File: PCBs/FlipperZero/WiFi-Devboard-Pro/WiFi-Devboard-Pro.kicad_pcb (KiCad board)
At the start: 2 copper layers, 78.5 x 20.1 mm, 46 parts, among them IC1 ESP32-WROOM-32E-N4, IC2 DMP1045U-7, IC3 AZ1117H-3.3TRE1, IC4 DMP1045U-7, IC5 DMP1045U-7, J1 3220-10-0300-00, J2 X6511WVS-08H-C60D48R2, J3 DZ254S-11-10-48, J4 Conn_01x11, J5 Conn_01x11, J6 503398-1892, U1 MMDT2907A-7-F, U2 MMDT2907A-7-F, U3 MMDT2907A-7-F

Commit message: started review
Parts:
- moved R6 1.29 mm to (150.1, 104.9), turned to 180 degrees
- moved C7 0.95 mm to (116.5, 92.3)
- moved R3 0.89 mm to (119.9, 91.9)
- moved C9 0.15 mm to (134.4, 99.5)
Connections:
- J4 pad 1: +3V3 -> GND
- J4 pad 2: GND -> +3V3
- J5 pad 1: GPIO25 -> GND
- J5 pad 10: GND -> RX
- J5 pad 11: +5V -> TX
- J5 pad 2: GPIO26 -> +5V
- J5 pad 3: GPIO27 -> GPIO25
- J5 pad 4: GPIO32 -> GPIO26
- J5 pad 5: GPIO33 -> GPIO27
- J5 pad 6: GPIO34 -> GPIO32
- J5 pad 7: GPIO35 -> GPIO33
- J5 pad 8: RX -> GPIO34
- J5 pad 9: TX -> GPIO35
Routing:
- net +5V: track 65.4 -> 33.9 mm, vias 2 -> 3
- net GND: track 42.1 -> 14.5 mm, vias 19 -> 11
- net RX: track 66.4 -> 55.6 mm
- net +3V3: track 53.0 -> 43.9 mm, vias 21 -> 15
- net GPIO16: track 24.7 -> 15.7 mm, vias 0 -> 2
- net TX: track 58.2 -> 49.9 mm
- net GPIO25: track 39.7 -> 34.3 mm
- net GPIO26: track 35.5 -> 30.3 mm
- net GPIO27: track 31.4 -> 26.3 mm
- net GPIO33: track 29.6 -> 25.2 mm
- net GPIO35: track 27.0 -> 22.7 mm
- net GPIO32: track 33.7 -> 29.9 mm
- net GPIO34: track 31.1 -> 27.4 mm
- net +ext_3V3: track 44.0 -> 41.1 mm
- net GPIO04: track 57.4 -> 55.7 mm
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
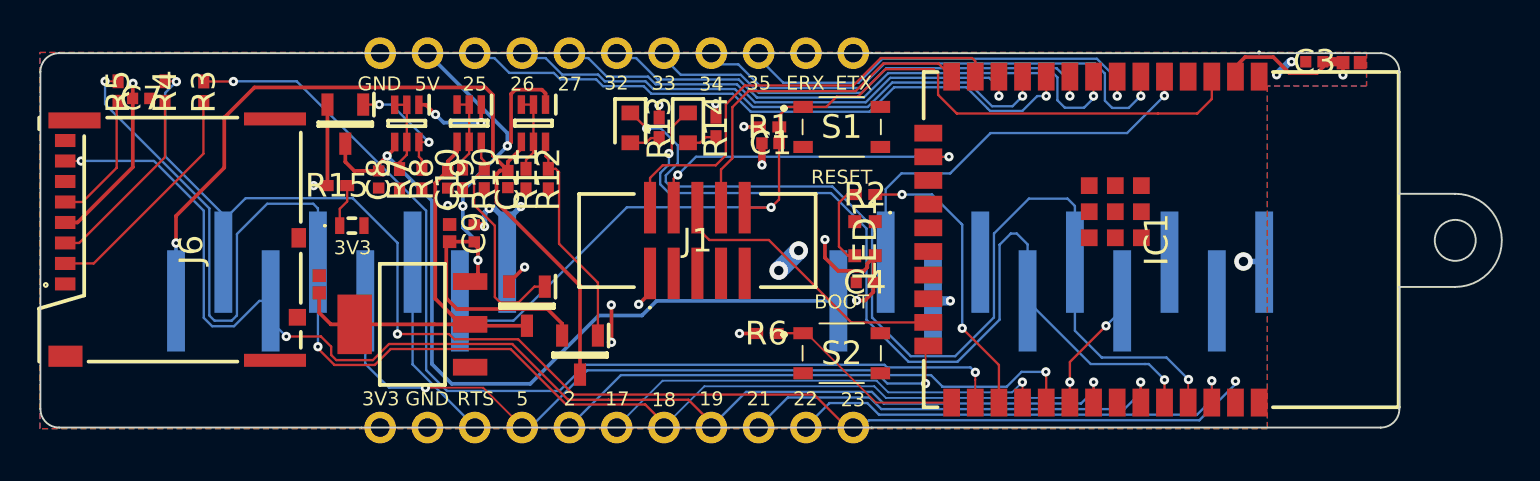
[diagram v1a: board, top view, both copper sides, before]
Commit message: rerouting done, continue with DRC
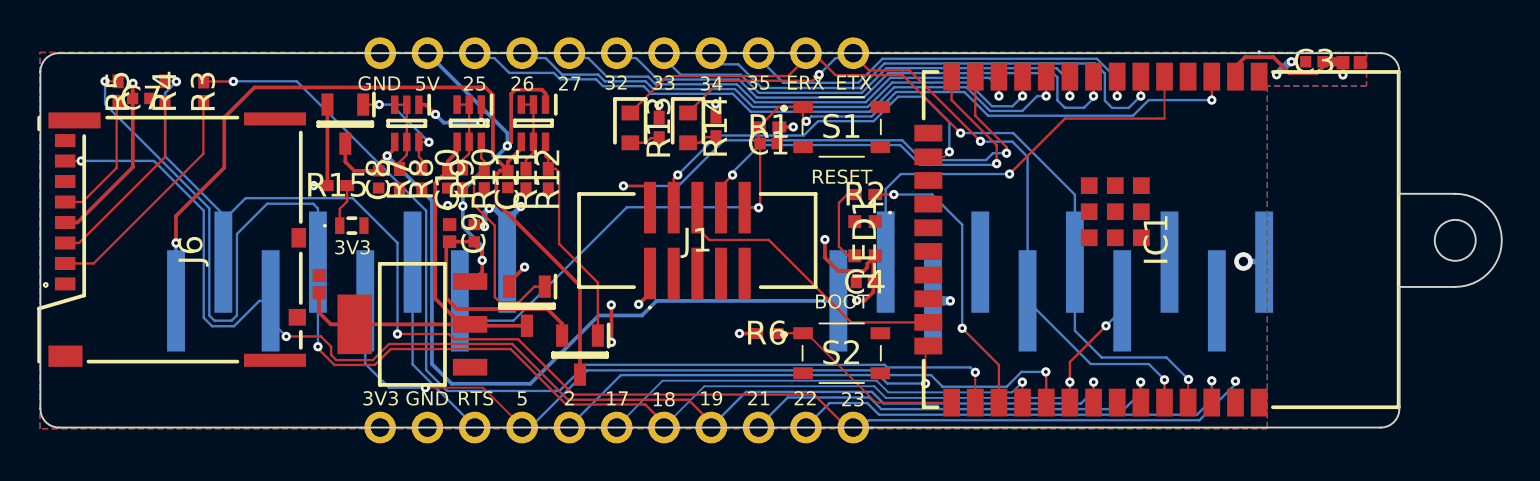
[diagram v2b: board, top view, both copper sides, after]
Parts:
- moved C1 0.10 mm to (150.2, 94.7), turned to 180 degrees
- turned R1 to 0 degrees
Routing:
- net RX: track 55.6 -> 43.7 mm
- net TX: track 49.9 -> 40.3 mm, vias 2 -> 3
- net TMS: track 24.2 -> 29.5 mm, vias 0 -> 2
- net TDI: track 18.7 -> 23.1 mm, vias 0 -> 2
- net TCK: track 17.9 -> 21.6 mm
- net GND: track 14.5 -> 11.8 mm, vias 11 -> 8
- net RESET: track 55.6 -> 52.9 mm, vias 1 -> 3
- net GPIO39: track 22.0 -> 22.7 mm

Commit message: Review complete, DRC done, ready for manufacturing, Tag: V0.1.0
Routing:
- net TMS: track 29.5 -> 25.2 mm
- net TCK: track 21.6 -> 17.4 mm
- net TDI: track 23.1 -> 19.6 mm
- net Net-(IC4-Pad1): track 12.2 -> 9.64 mm
- net RX: track 43.7 -> 45.5 mm
- net GND: track 11.8 -> 13.5 mm, vias 8 -> 7
- net GPIO23: track 77.9 -> 79.0 mm
- net GPIO05: track 44.8 -> 44.2 mm
- net GPIO39: track 22.7 -> 22.1 mm
- net +5V: vias 3 -> 2
